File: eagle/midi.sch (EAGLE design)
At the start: 29 parts, among them CON1 EXPANSION-PORT, IC1 74LS14, IC2 6N138, IC4 74LS02, IC5 74LS74, IC6 74AHCT1G32DBV, IC7 74LS273, IC8 SST39SF040, IC9 74LS00D, Q1 2MHz

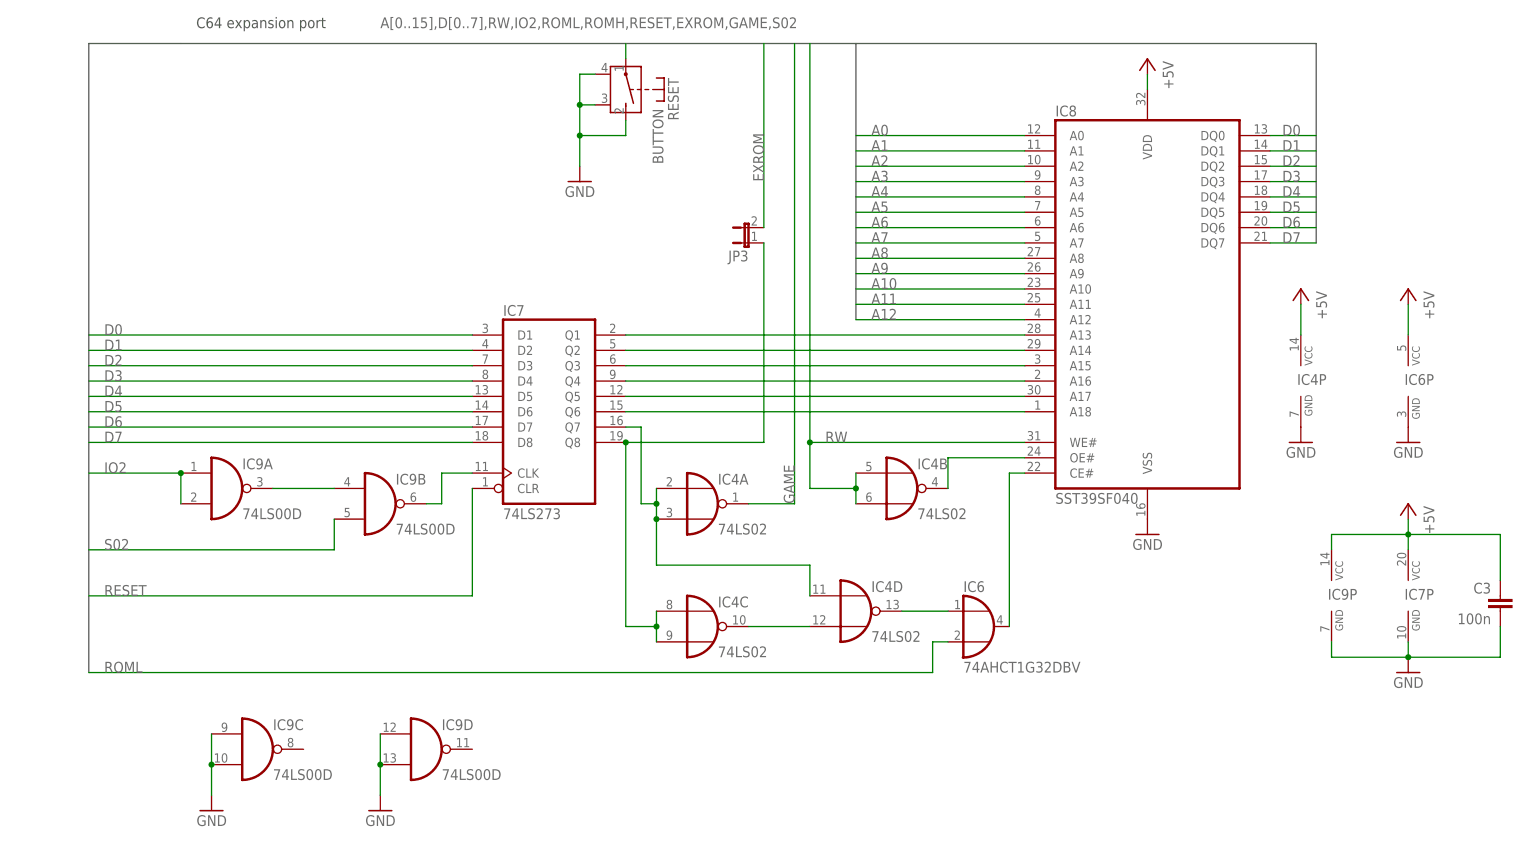
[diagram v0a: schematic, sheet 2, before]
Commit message: version 0.5 with additonal 74LS00
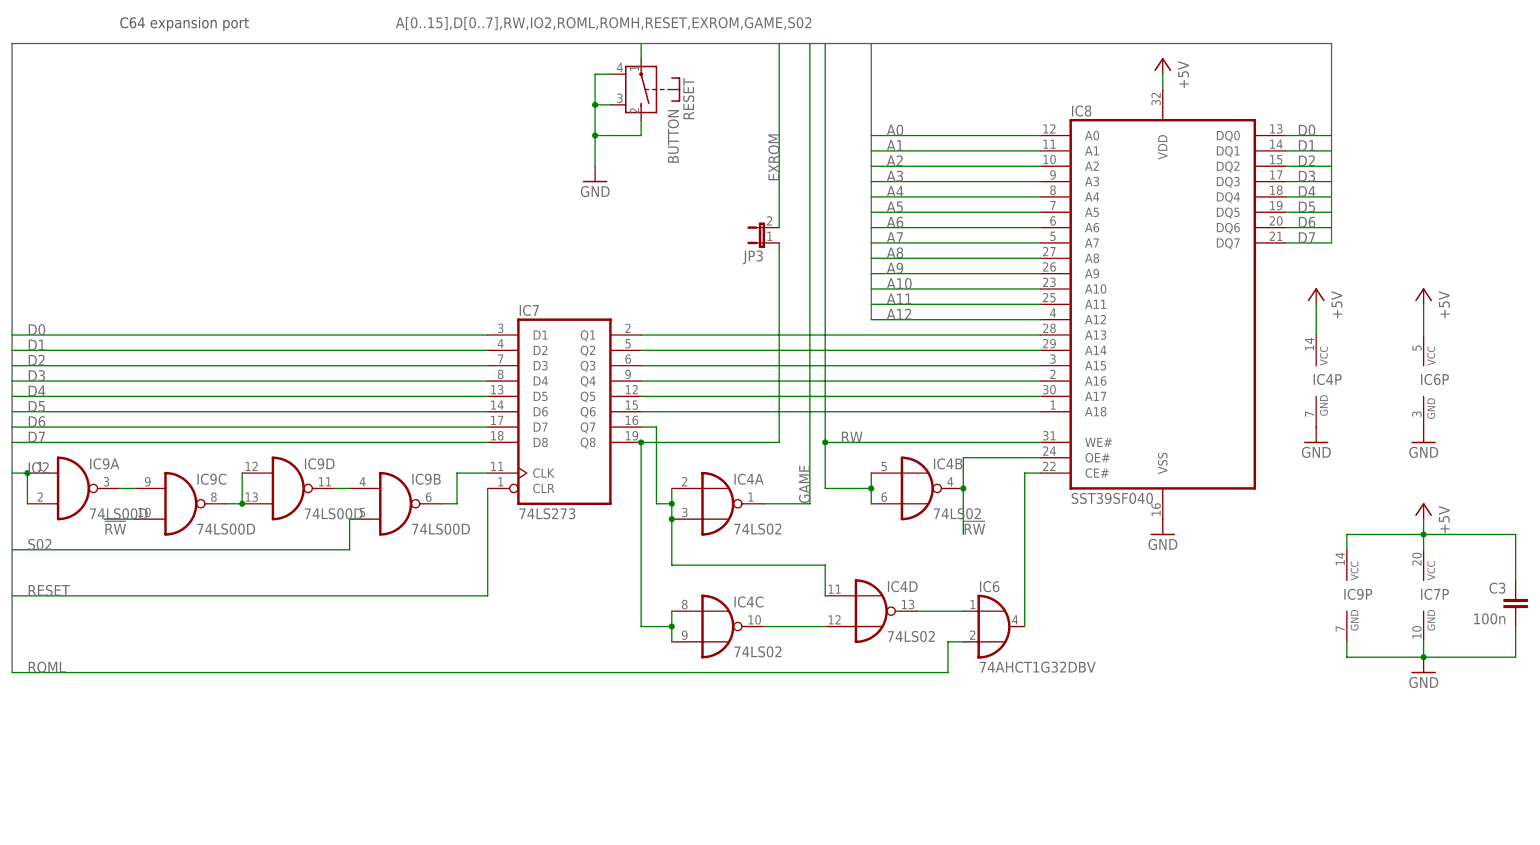
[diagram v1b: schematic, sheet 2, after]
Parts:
- added C4: 10u, rcl:C-EU050-035X075
- added Q2: DMP2100U, transistor-power:FDN360P
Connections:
- removed net OE: IC4B.O, IC8.OE#
- removed net ROMH: CON1.!ROMH
- new net !RW: IC4B.O, IC8.OE#, IC9C.I1
- new net 5V-SW: C1.1, IC3A.CS0, IC3A.CS1, IC3P.VCC, IC5A.CLR, IC5A.PRE, IC5B.CLR, IC5B.PRE, IC5P.VCC, Q1.VCC, Q2.D
- new net N$30: IC9B.I0, IC9D.O
- new net N$35: IC1B.O, Q2.G
- new net N$9: IC9C.O, IC9D.I0, IC9D.I1
- net +5V: now also C4.1, Q2.S; no longer C1.1, IC3A.CS0, IC3A.CS1, IC3P.VCC, IC5A.CLR, IC5A.PRE, IC5B.CLR, IC5B.PRE, IC5P.VCC, Q1.VCC
- net GND: now also C4.2; no longer IC1B.I, IC9C.I0, IC9C.I1, IC9D.I0, IC9D.I1
- net N$8: now also IC9C.I0; no longer IC9B.I0
- net RESET: now also IC1B.I
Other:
- moved on the sheet: C1, C2, C3, IC1B, IC1P, IC3P, IC4A, IC4B, IC4C, IC4D, IC4P, IC6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

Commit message: revision 1.0
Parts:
- added C10, C5, C6, C7, C8, C9: 100n, rcl:C-EUC0805
- added C11, C12: 1n, rcl:C-EUC0805
- added D2, D3: BAV99, diode:BAV199
- added R7: 10k, rcl:R-EU_R0805
- C1, C2, C3: device rcl:C-EU025-025X050 -> rcl:C-EUC0805
- C4: device rcl:C-EU050-035X075 -> rcl:C-EUC0805
- D1: value 1N914 -> BAV99; device diode:1N4148DO35-7 -> diode:BAV199
- R1, R2, R3, R4, R5, R6: device rcl:R-EU_0204/7 -> rcl:R-EU_R1206
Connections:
- removed net N$2: D1.C, IC2.A, R4.1
- new net N$37: D1.AC, D1.C, IC2.A, R4.1
- net +5V: now also C10.1, C7.1, C8.1, C9.1, D2.C, D3.C, R7.1
- net 5V-SW: now also C5.1, C6.1
- net GND: now also C10.2, C11.2, C12.2, C5.2, C6.2, C7.2, C8.2, C9.2, D2.A, D3.A
- net N$16: now also C12.1, D3.AC
- net N$28: now also C11.1, D2.AC
- net N$35: now also R7.2
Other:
- moved on the sheet: IC1D, IC1E, R1, R2

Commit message: circuit rev B with CPLD
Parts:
- removed C10, C2, C5, C6, C7, C8, C9: 100n, rcl:C-EUC0805
- removed C11, C12: 1n, rcl:C-EUC0805
- removed C4: 10u, rcl:C-EUC0805
- removed CON1: EXPANSION-PORT, cartridge:EXPANSION-PORT
- removed D1, D2, D3: BAV99, diode:BAV199
- removed IC6: 74AHCT1G32DBV, 74xx-little-de:74AHCT1G32DBV
- removed IC7: 74LS273, 74xx-eu:74AC273DW
- removed IC8: SST39SF040, flash:SST39SF040
- removed IC9: 74LS00D, 74xx-eu:74LS00D
- removed JP2, JP4: (no value), jumper:JP2E
- removed JP3: (no value), jumper:JP1E
- removed Q1: 2MHz, crystal:XO-14
- removed Q2: DMP2100U, transistor-power:FDN360P
- removed RESET: BUTTON, button:BUTTON
- added 3V3, AUX, GND, TCK, TDI, TDO, TMS: LSP10, solpad:LSP10
- added C13, C14, C17, C18, C19, C20, C21, C26, C28, C37: 100n, rcl:C-EUC0402
- added C15, C16: 1n, rcl:C-EUC0402
- added C22: 10u, rcl:C-EUC0805
- added C24: 1u, rcl:C-EUC0805
- added CON2: EXPANSION-PORT, cartridge:EXPANSION-PORT
- added D4, D5, D6: BAV99, diode:BAV199
- added IC11: (no value), micro-motorola:6850
- added IC12: 74LS14, 74xx-eu:74LS14D
- added IC16: 74LVC8T245, 74lvc8t245:74LVC8T245
- added IC18: MCP1703CB, linear:MCP1703CB
- added LED1, LED2: (no value), led:LED3MM
- added R10, R11, R12, R13, R8, R9: 220, rcl:R-EU_R1206
- added R14, R17, R18: 10k, rcl:R-EU_R0402
- added R15, R16: 4k7, rcl:R-EU_R0402
- added RESET1: BUTTON, button:BUTTON
- C1, C3: device rcl:C-EUC0805 -> rcl:C-EUC0402
- IC1: value 74LS14 -> SST39VF1681; device 74xx-eu:74LS14D -> flash:SST39VF1681
- IC2: value 6N138 -> XC9572XL_TQ100; device optocoupler:6N138 -> xc9572xl-tq100:XC9572XL_TQ100
- IC3: value (none) -> 6N138SMD; device micro-motorola:6850 -> 6n138:6N138SMD
- IC4: value 74LS02 -> 12MHz; device 74xx-eu:74AC02D -> cartridge:ASE
- IC5: value 74LS74 -> CY61228EV30; device 74xx-eu:74LS74D -> CY62128EV30:CY61228EV30
- JP1: device jumper:JP2E -> jumper:JP1E
- R1, R2, R3: value 220 -> 10k; device rcl:R-EU_R1206 -> rcl:R-EU_R0402
- R4, R5: value 220 -> 1k; device rcl:R-EU_R1206 -> rcl:R-EU_R0402
- R6: value 330 -> 10k; device rcl:R-EU_R1206 -> rcl:R-EU_R0402
- R7: value 10k -> 220; device rcl:R-EU_R0805 -> rcl:R-EU_R1206
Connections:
- removed net !RW: IC4B.O, IC8.OE#, IC9C.I1
- removed net 5V-SW: C1.1, C5.1, C6.1, IC3A.CS0, IC3A.CS1, IC3P.VCC, IC5A.CLR, IC5A.PRE, IC5B.CLR, IC5B.PRE, IC5P.VCC, Q1.VCC, Q2.D
- removed net CE: IC6A.O, IC8.CE#
- removed net N$10: IC1D.O, R2.2
- removed net N$11: IC1E.I, JP1.2
- removed net N$12: IC1E.O, R1.2
- removed net N$14: IC3A.RXCLK, IC3A.TXCLK, JP2.2
- removed net N$15: IC1C.O, IC3A.RXDATA
- removed net N$16: C12.1, D3.AC, OUT.5, R2.1
- removed net N$17: IC7A.Q1, IC8.A13
- removed net N$19: IC7A.Q3, IC8.A15
- removed net N$20: IC7A.Q4, IC8.A16
- removed net N$21: IC7A.Q5, IC8.A17
- removed net N$22: IC7A.Q6, IC8.A18
- removed net N$23: IC7A.CLK, IC9B.O
- removed net N$24: IC4C.O, IC4D.I1
- removed net N$25: IC1A.I, IC3A.TXDATA
- removed net N$26: CON1.!IRQ, JP4.3
- removed net N$27: CON1.!NMI, JP4.1
- removed net N$28: C11.1, D2.AC, R1.1, THRU.5
- removed net N$29: IC4D.O, IC6A.I0
- removed net N$30: IC9B.I0, IC9D.O
- removed net N$31: IC5A.!Q, IC5A.D
- removed net N$32: IC5B.!Q, IC5B.D
- removed net N$33: IC5A.CLK, JP2.1, Q1.OUT
- removed net N$34: IC5A.Q, IC5B.CLK
- removed net N$35: IC1B.O, Q2.G, R7.2
- removed net N$36: IC5B.Q, JP2.3
- removed net N$37: D1.AC, D1.C, IC2.A, R4.1
- removed net N$9: IC9C.O, IC9D.I0, IC9D.I1
- removed net Q7: IC4A.I0, IC4A.I1, IC4D.I0, IC7A.Q7
- removed net Q8: IC4C.I0, IC4C.I1, IC7A.Q8, JP3.1
- new net +3V3: 3V3.MP, C1.1, C17.1, C18.1, C19.1, C24.1, C26.1, C28.1, C3.1, C37.1, IC1.!RST, IC1.VDD@1, IC16.VCCA, IC18.VO, IC2.VCCINT_1, IC2.VCCINT_2, IC2.VCCINT_VPP, IC2.VCCIO_1, IC2.VCCIO_2, IC2.VCCIO_3, IC2.VCCIO_4, IC4.VDD, IC5.CE2, IC5.VCC, R14.2, R15.1, R16.1, R18.2, R2.1
- new net 6850-CS2: IC11A.CS2, IC2.PB02_12, R1.1
- new net 6850-IRQ: IC11A.IRQ, IC2.PB02_16
- new net 6850-RS: IC11A.RS, IC2.PB02_15
- new net 6850-RW: IC11A.R/!W, IC2.PB03_00
- new net 6850-RX/TX-CLK: IC11A.RXCLK, IC11A.TXCLK, IC2.PB02_13
- new net 6850-RXDATA: IC11A.RXDATA, IC12F.O, IC2.PB02_06
- new net 6850-TXDATA: IC11A.TXDATA, IC12E.I, IC2.PB02_14
- new net A13: CON2.A13, IC2.PB03_06
- new net A14: CON2.A14, IC2.PB03_10
- new net A15: CON2.A15, IC2.PB03_02
- new net AT0: IC1.A0, IC2.PB00_04, IC5.A0
- new net AT1: IC1.A1, IC2.PB00_01, IC5.A1
- new net AT10: IC1.A10, IC2.PB00_00, IC5.A10
- new net AT11: IC1.A11, IC2.PB00_08, IC5.A14
- new net AT12: IC1.A12, IC2.PB00_10, IC5.A12
- new net AT13: IC1.A13, IC2.PB00_06, IC5.A7
- new net AT14: IC1.A14, IC2.PB00_09, IC5.A6
- new net AT15: IC1.A15, IC2.PB00_14, IC5.A5
- new net AT16: IC1.A16, IC2.PB00_16, IC5.A4
- new net AT17: IC1.A17, IC2.PB02_17
- new net AT18: IC1.A18, IC2.PB02_07
- new net AT19: IC1.A19, IC2.PB00_12
- new net AT2: IC1.A2, IC2.PB01_16, IC5.A2
- new net AT20: IC1.A20, IC2.PB00_11
- new net AT3: IC1.A3, IC2.PB01_14, IC5.A3
- new net AT4: IC1.A4, IC2.PB00_03, IC5.A16
- new net AT5: IC1.A5, IC2.PB02_08, IC5.A11
- new net AT6: IC1.A6, IC2.PB02_00, IC5.A9
- new net AT7: IC1.A7, IC2.PB00_17, IC5.A8
- new net AT8: IC1.A8, IC2.PB00_15, IC5.A13
- new net AT9: IC1.A9, IC2.PB02_01, IC5.A15
- new net BA: CON2.BA
- new net DIR: IC16.DIR, IC2.PB01_09, R17.1
- new net DMA: CON2.!DMA
- new net DOT-CLOCK: CON2.DOT-CLOCK
- new net DT0: IC1.D0, IC16.A1, IC2.PB01_06, IC5.D7
- new net DT1: IC1.D1, IC16.A2, IC2.PB01_10, IC5.D6
- new net DT2: IC1.D2, IC16.A3, IC2.PB01_11, IC5.D5
- new net DT3: IC1.D3, IC16.A4, IC2.PB01_12, IC5.D4
- new net DT4: IC1.D4, IC16.A5, IC2.PB01_13, IC5.D3
- new net DT5: IC1.D5, IC16.A6, IC2.PB01_15, IC5.D2
- new net DT6: IC1.D6, IC16.A7, IC2.PB00_02, IC5.D1
- new net DT7: IC1.D7, IC16.A8, IC2.PB00_07, IC5.D0
- new net FLASH-CE: IC1.!CE, IC2.PB02_09, R14.1
- new net LED1: IC2.PB02_05, R4.1
- new net LED2: IC2.PB02_10, R5.1
- new net MIDI-OUT-INVERTED: IC12C.I, IC12E.O
- new net MIDI-THRU: IC12A.I, IC2.PB02_02
- new net N$2: IC2.PB00_13, IC4.OUT
- new net N$38: IN.4, R8.2
- new net N$39: IC12D.I, IC3.VO, R7.2
- new net N$40: OUT.4, R11.1
- new net N$41: R10.1, THRU.4
- new net N$42: C16.1, D6.AC, OUT.5, R13.1
- new net N$43: C15.1, D5.AC, R12.1, THRU.5
- new net N$44: IC12C.O, R13.2
- new net N$45: IC12B.O, R12.2
- new net N$47: D4.A, IC3.C, IN.5
- new net N$48: D4.AC, D4.C, IC3.A, R8.1
- new net NMI: CON2.!NMI, IC2.PB03_04
- new net OE: IC1.!OE, IC2.PB02_11, IC5.!OE
- new net RAM-CE: IC2.PB00_05, IC5.!CE1, R18.1
- new net ROMH: CON2.!ROMH, IC2.PB03_08
- new net TCK: IC2.TCK, TCK.MP
- new net TDI: IC2.TDI, R15.2, TDI.MP
- new net TDO: IC2.TDO, TDO.MP
- new net TMS: IC2.TMS, R16.2, TMS.MP
- new net WE: IC1.!WE, IC2.PB02_04, IC5.!WE
- net +5V: now also C13.1, C14.1, C20.1, C21.1, C22.1, CON2.+5V1, CON2.+5V2, D5.C, D6.C, IC11A.CS0, IC11A.CS1, IC11P.VCC, IC12P.VCC, IC16.VCCB, IC16.VCCB2, IC18.VI, IC3.VCC, R1.2, R10.2, R11.2, R9.1; no longer C10.1, C2.1, C3.1, C4.1, C7.1, C8.1, C9.1, CON1.+5V1, CON1.+5V2, D2.C, D3.C, IC1P.VCC, IC2.VCC, IC4P.VCC, IC6P.VCC, IC7P.VCC, IC8.VDD, IC9P.VCC, Q2.S, R3.2, R5.2, R6.2, R7.1
- net A0: now also CON2.A0, IC2.PB01_08; no longer CON1.A0, IC3A.RS, IC8.A0
- net A1: now also CON2.A1, IC2.PB01_07; no longer CON1.A1, IC8.A1
- net A10: now also CON2.A10, IC2.PB03_15; no longer CON1.A10, IC8.A10
- net A11: now also CON2.A11, IC2.PB03_11; no longer CON1.A11, IC8.A11
- net A12: now also CON2.A12, IC2.PB03_17; no longer CON1.A12, IC8.A12
- net A2: now also CON2.A2, IC2.PB01_05; no longer CON1.A2, IC8.A2
- net A3: now also CON2.A3, IC2.PB01_04; no longer CON1.A3, IC8.A3
- net A4: now also CON2.A4, IC2.PB01_01; no longer CON1.A4, IC8.A4
- net A5: now also CON2.A5, IC2.PB01_03; no longer CON1.A5, IC8.A5
- net A6: now also CON2.A6, IC2.PB01_17; no longer CON1.A6, IC8.A6
- net A7: now also CON2.A7, IC2.PB01_02; no longer CON1.A7, IC8.A7
- net A8: now also CON2.A8, IC2.PB03_16; no longer CON1.A8, IC8.A8
- net A9: now also CON2.A9, IC2.PB03_14; no longer CON1.A9, IC8.A9
- net D0: now also CON2.D0, IC11A.D0, IC16.B1; no longer CON1.D0, IC3A.D0, IC7A.D1, IC8.DQ0
- net D1: now also CON2.D1, IC11A.D1, IC16.B2; no longer CON1.D1, IC3A.D1, IC7A.D2, IC8.DQ1
- net D2: now also CON2.D2, IC11A.D2, IC16.B3; no longer CON1.D2, IC3A.D2, IC7A.D3, IC8.DQ2
- net D3: now also CON2.D3, IC11A.D3, IC16.B4; no longer CON1.D3, IC3A.D3, IC7A.D4, IC8.DQ3
- net D4: now also CON2.D4, IC11A.D4, IC16.B5; no longer CON1.D4, IC3A.D4, IC7A.D5, IC8.DQ4
- net D5: now also CON2.D5, IC11A.D5, IC16.B6; no longer CON1.D5, IC3A.D5, IC7A.D6, IC8.DQ5
- net D6: now also CON2.D6, IC11A.D6, IC16.B7; no longer CON1.D6, IC3A.D6, IC7A.D7, IC8.DQ6
- net D7: now also CON2.D7, IC11A.D7, IC16.B8; no longer CON1.D7, IC3A.D7, IC7A.D8, IC8.DQ7
- net EXROM: now also CON2.!EXROM, JP1.1; no longer CON1.!EXROM, JP3.2
- net GAME: now also CON2.!GAME, IC2.PB03_13; no longer CON1.!GAME, IC4A.O
- net GND: now also C13.2, C14.2, C15.2, C16.2, C17.2, C18.2, C19.2, C20.2, C21.2, C22.2, C24.2, C26.2, C28.2, C37.2, CON2.GND1, CON2.GND2, CON2.GND3, CON2.GND4, D5.A, D6.A, GND.MP, IC1.GND@1, IC1.GND@2, IC11A.CTS, IC11A.DCD, IC11P.VSS, IC12P.GND, IC16.GND, IC16.GND2, IC16.GND3, IC16.OE, IC18.GND, IC2.VSSINT_1, IC2.VSSINT_2, IC2.VSSINT_3, IC2.VSSIO_1, IC2.VSSIO_2, IC2.VSSIO_3, IC2.VSSIO_4, IC2.VSSIO_5, IC3.GND, IC4.GND, IC5.GND, LED1.C, LED2.C, R17.2, R3.2, R6.1, RESET1.2, RESET1.3, RESET1.4; no longer C10.2, C11.2, C12.2, C2.2, C4.2, C5.2, C6.2, C7.2, C8.2, C9.2, CON1.GND1, CON1.GND2, CON1.GND3, CON1.GND4, D2.A, D3.A, IC1P.GND, IC2.GND, IC3A.CTS, IC3A.DCD, IC3P.VSS, IC4P.GND, IC5P.GND, IC6P.GND, IC7P.GND, IC8.VSS, IC9P.GND, Q1.GND, RESET.2, RESET.3, RESET.4
- net IO1: now also CON2.I/O1, IC2.PB03_05; no longer CON1.I/O1, IC3A.CS2
- net IO2: now also CON2.I/O2, IC2.PB03_12; no longer CON1.I/O2, IC9A.I0, IC9A.I1
- net IRQ: now also CON2.!IRQ, IC2.PB03_07; no longer IC3A.IRQ, JP4.2
- net N$1: now also IC3.VB, R6.2; no longer IN.4, R4.2
- net N$13: now also IC1.!WP, R2.2, R3.1; no longer IC1A.O, IC1D.I, JP1.3
- net N$18: now also LED2.A, R5.2; no longer IC7A.Q2, IC8.A14
- net N$3: now also R7.1, R9.2; no longer D1.A, IC2.C, IN.5
- net N$4: now also IC12A.O, IC12B.I; no longer IC1F.I, IC2.VO, R6.1
- net N$5: now also IC12D.O, IC12F.I; no longer IC1C.I, IC1F.O, JP1.1
- net N$6: now also LED1.A, R4.2; no longer OUT.4, R3.1
- net N$7: now also IC2.PB03_09, JP1.2; no longer R5.1, THRU.4
- net N$8: now also AUX.MP, IC2.PB02_03; no longer IC9A.O, IC9C.I0
- net RESET: now also CON2.!RESET, IC2.PB03_01, RESET1.1; no longer CON1.!RESET, IC1B.I, IC7A.CLR, RESET.1
- net ROML: now also CON2.!ROML, IC2.PB01_00; no longer CON1.!ROML, IC6A.I1
- net RW: now also CON2.R/W, IC2.PB03_03; no longer CON1.R/W, IC3A.R/!W, IC4B.I0, IC4B.I1, IC8.WE#
- net S02: now also CON2.S02, IC11A.E; no longer CON1.S02, IC3A.E, IC9B.I1

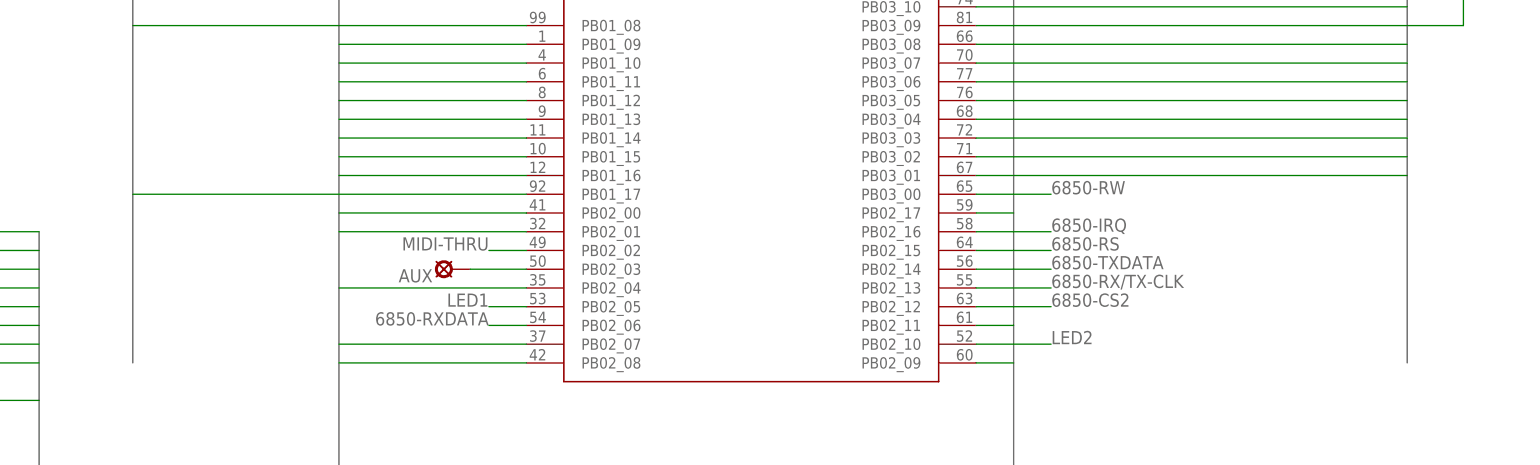
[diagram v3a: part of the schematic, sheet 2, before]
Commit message: first working prototype with CPLD
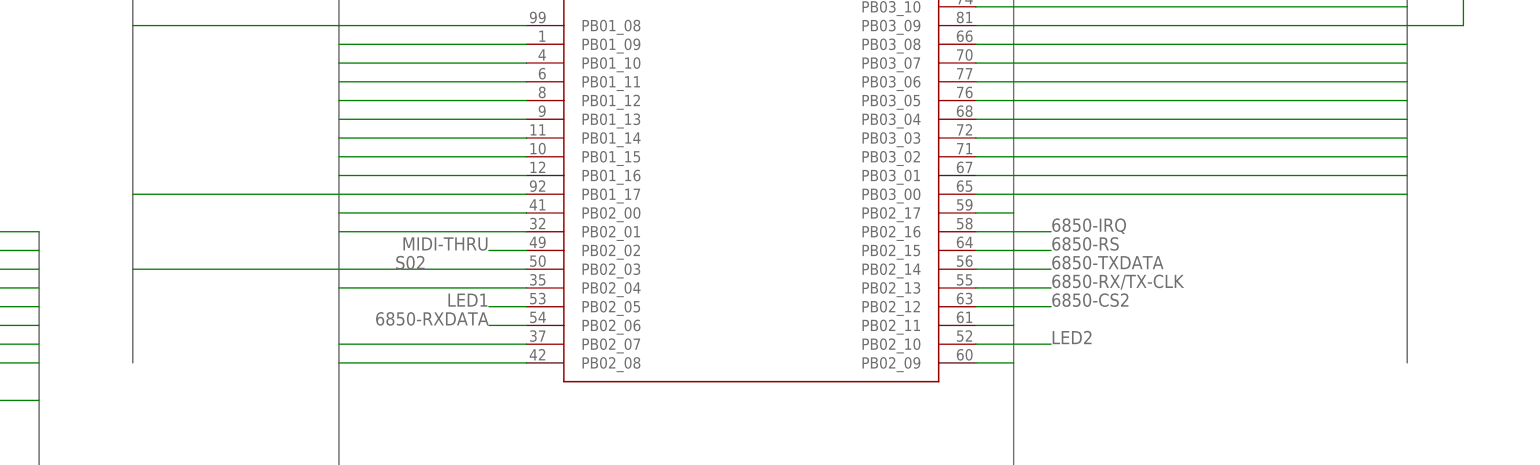
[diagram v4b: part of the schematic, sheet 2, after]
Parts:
- removed AUX: LSP10, solpad:LSP10
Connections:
- removed net 6850-RW: IC11A.R/!W, IC2.PB03_00
- removed net N$8: AUX.MP, IC2.PB02_03
- net BA: now also IC2.PB03_00
- net RW: now also IC11A.R/!W
- net S02: now also IC2.PB02_03

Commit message: new 4 layer board
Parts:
- removed C17, C18, C19, C20, C21, C26, C28, C37: 100n, rcl:C-EUC0402
- removed C22: 10u, rcl:C-EUC0805
- removed IC12: 74LS14, 74xx-eu:74LS14D
- removed IC16: 74LVC8T245, 74lvc8t245:74LVC8T245
- removed IC18: MCP1703CB, linear:MCP1703CB
- removed RESET1: BUTTON, button:BUTTON
- added C10, C12, C4, C5, C6, C7, C8, C9: 100n, rcl:C-EUC0603
- added C2: 1n, rcl:C-EUC0603
- added IC10: EMI-FILTER, emv-filter:EMV-FILTER
- added IC6: XC95144XL_TQ100, xc9572xl-tq100:XC9572XL_TQ100
- added IC7: (no value), micro-motorola:6850
- added IC8: MCP1703DB, mcp1703:MCP1703DB
- added IC9: 74LVC8T245, 74lvc8t245:74LVC8T245
- added R19: 10k, rcl:R-EU_R0603
- added RESET: BUTTON, button:BUTTON
- C1: value 100n -> 1n; device rcl:C-EUC0402 -> rcl:C-EUC0603
- C13, C3: device rcl:C-EUC0402 -> rcl:C-EUC0603
- C14: value 100n -> 10u; device rcl:C-EUC0402 -> rcl:C-EUC0805
- C15, C16: value 1n -> 100n; device rcl:C-EUC0402 -> rcl:C-EUC0603
- IC1: value SST39VF1681 -> 74LS14; device flash:SST39VF1681 -> 74xx-eu:74LS14D
- IC11: value (none) -> EMI-FILTER; device micro-motorola:6850 -> emv-filter:EMV-FILTER
- IC2: value XC9572XL_TQ100 -> SST39VF1681; device xc9572xl-tq100:XC9572XL_TQ100 -> flash:SST39VF1681
- IC4: value 12MHz -> 48MHz
- R1, R2, R3: value 10k -> 220; device rcl:R-EU_R0402 -> rcl:R-EU_R1206
- R10, R12, R8: value 220 -> 10k; device rcl:R-EU_R1206 -> rcl:R-EU_R0603
- R13: value 220 -> 4k7; device rcl:R-EU_R1206 -> rcl:R-EU_R0603
- R14, R17: value 10k -> 4k7; device rcl:R-EU_R0402 -> rcl:R-EU_R0603
- R15, R16: value 4k7 -> 10k; device rcl:R-EU_R0402 -> rcl:R-EU_R0603
- R18: device rcl:R-EU_R0402 -> rcl:R-EU_R0603
- R4, R5: value 1k -> 220; device rcl:R-EU_R0402 -> rcl:R-EU_R1206
- R6: value 10k -> 1k; device rcl:R-EU_R0402 -> rcl:R-EU_R0603
- R7: value 220 -> 1k; device rcl:R-EU_R1206 -> rcl:R-EU_R0603
- renumbered C24 to C11, CON2 to CON1, D4 to D3, D5 to D1, D6 to D2
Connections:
- new net EXROM-F: IC11.10, JP1.1
- new net GAME-F: IC11.12, IC6.PB03_13
- new net IRQ-F: IC11.16, IC6.PB03_07
- new net N$10: IC10.6, IC9.B6
- new net N$11: IC10.5, IC9.B5
- new net N$12: IC10.4, IC9.B4
- new net N$14: IC10.3, IC9.B3
- new net N$15: IC10.2, IC9.B2
- new net N$16: IC10.1, IC9.B1
- new net N$8: IC10.8, IC9.B8
- new net N$9: IC10.7, IC9.B7
- new net NMI-F: IC11.14, IC6.PB03_04
- net +3V3: now also C10.1, C12.1, C13.1, C6.1, C7.1, C8.1, C9.1, IC2.!RST, IC2.VDD@1, IC6.VCCINT_1, IC6.VCCINT_2, IC6.VCCINT_VPP, IC6.VCCIO_1, IC6.VCCIO_2, IC6.VCCIO_3, IC6.VCCIO_4, IC8.VO, IC9.VCCA, R12.2, R13.1, R14.1, R15.2; no longer C1.1, C17.1, C18.1, C19.1, C26.1, C28.1, C37.1, IC1.!RST, IC1.VDD@1, IC16.VCCA, IC18.VO, IC2.VCCINT_1, IC2.VCCINT_2, IC2.VCCINT_VPP, IC2.VCCIO_1, IC2.VCCIO_2, IC2.VCCIO_3, IC2.VCCIO_4, R14.2, R15.1, R16.1, R18.2, R2.1
- net +5V: now also C15.1, C16.1, C4.1, C5.1, IC1P.VCC, IC7A.CS0, IC7A.CS1, IC7P.VCC, IC8.VI, IC9.VCCB, IC9.VCCB2, R17.2, R18.2, R4.2; no longer C13.1, C20.1, C21.1, C22.1, IC11A.CS0, IC11A.CS1, IC11P.VCC, IC12P.VCC, IC16.VCCB, IC16.VCCB2, IC18.VI, R10.2, R11.2
- net 6850-CS2: now also IC6.PB02_12, IC7A.CS2, R18.1; no longer IC11A.CS2, IC2.PB02_12, R1.1
- net 6850-IRQ: now also IC6.PB02_16, IC7A.IRQ, R17.1; no longer IC11A.IRQ, IC2.PB02_16
- net 6850-RS: now also IC6.PB02_15, IC7A.RS; no longer IC11A.RS, IC2.PB02_15
- net 6850-RX/TX-CLK: now also IC6.PB02_13, IC7A.RXCLK, IC7A.TXCLK; no longer IC11A.RXCLK, IC11A.TXCLK, IC2.PB02_13
- net 6850-RXDATA: now also IC1F.O, IC6.PB02_06, IC7A.RXDATA; no longer IC11A.RXDATA, IC12F.O, IC2.PB02_06
- net 6850-TXDATA: now also IC1E.I, IC6.PB02_14, IC7A.TXDATA; no longer IC11A.TXDATA, IC12E.I, IC2.PB02_14
- net A0: now also IC6.PB01_08; no longer IC2.PB01_08
- net A1: now also IC6.PB01_07; no longer IC2.PB01_07
- net A10: now also IC6.PB03_15; no longer IC2.PB03_15
- net A11: now also IC6.PB03_11; no longer IC2.PB03_11
- net A12: now also IC6.PB03_17; no longer IC2.PB03_17
- net A13: now also IC6.PB03_06; no longer IC2.PB03_06
- net A14: now also IC6.PB03_10; no longer IC2.PB03_10
- net A15: now also IC6.PB03_02; no longer IC2.PB03_02
- net A2: now also IC6.PB01_05; no longer IC2.PB01_05
- net A3: now also IC6.PB01_04; no longer IC2.PB01_04
- net A4: now also IC6.PB01_01; no longer IC2.PB01_01
- net A5: now also IC6.PB01_03; no longer IC2.PB01_03
- net A6: now also IC6.PB01_17; no longer IC2.PB01_17
- net A7: now also IC6.PB01_02; no longer IC2.PB01_02
- net A8: now also IC6.PB03_16; no longer IC2.PB03_16
- net A9: now also IC6.PB03_14; no longer IC2.PB03_14
- net AT0: now also IC2.A0, IC6.PB00_04; no longer IC1.A0, IC2.PB00_04
- net AT1: now also IC2.A1, IC6.PB00_01; no longer IC1.A1, IC2.PB00_01
- net AT10: now also IC2.A10, IC6.PB00_00; no longer IC1.A10, IC2.PB00_00
- net AT11: now also IC2.A11, IC6.PB00_08; no longer IC1.A11, IC2.PB00_08
- net AT12: now also IC2.A12, IC6.PB00_10; no longer IC1.A12, IC2.PB00_10
- net AT13: now also IC2.A13, IC6.PB00_06; no longer IC1.A13, IC2.PB00_06
- net AT14: now also IC2.A14, IC6.PB00_09; no longer IC1.A14, IC2.PB00_09
- net AT15: now also IC2.A15, IC6.PB00_14; no longer IC1.A15, IC2.PB00_14
- net AT16: now also IC2.A16, IC6.PB00_16; no longer IC1.A16, IC2.PB00_16
- net AT17: now also IC2.A17, IC6.PB02_17; no longer IC1.A17, IC2.PB02_17
- net AT18: now also IC2.A18, IC6.PB02_07; no longer IC1.A18, IC2.PB02_07
- net AT19: now also IC2.A19, IC6.PB00_12; no longer IC1.A19, IC2.PB00_12
- net AT2: now also IC2.A2, IC6.PB01_16; no longer IC1.A2, IC2.PB01_16
- net AT20: now also IC2.A20, IC6.PB00_11; no longer IC1.A20, IC2.PB00_11
- net AT3: now also IC2.A3, IC6.PB01_14; no longer IC1.A3, IC2.PB01_14
- net AT4: now also IC2.A4, IC6.PB00_03; no longer IC1.A4, IC2.PB00_03
- net AT5: now also IC2.A5, IC6.PB02_08; no longer IC1.A5, IC2.PB02_08
- net AT6: now also IC2.A6, IC6.PB02_00; no longer IC1.A6, IC2.PB02_00
- net AT7: now also IC2.A7, IC6.PB00_17; no longer IC1.A7, IC2.PB00_17
- net AT8: now also IC2.A8, IC6.PB00_15; no longer IC1.A8, IC2.PB00_15
- net AT9: now also IC2.A9, IC6.PB02_01; no longer IC1.A9, IC2.PB02_01
- net BA: now also IC6.PB03_00; no longer IC2.PB03_00
- net D0: now also IC10.16, IC7A.D0; no longer IC11A.D0, IC16.B1
- net D1: now also IC10.15, IC7A.D1; no longer IC11A.D1, IC16.B2
- net D2: now also IC10.14, IC7A.D2; no longer IC11A.D2, IC16.B3
- net D3: now also IC10.13, IC7A.D3; no longer IC11A.D3, IC16.B4
- net D4: now also IC10.12, IC7A.D4; no longer IC11A.D4, IC16.B5
- net D5: now also IC10.11, IC7A.D5; no longer IC11A.D5, IC16.B6
- net D6: now also IC10.10, IC7A.D6; no longer IC11A.D6, IC16.B7
- net D7: now also IC10.9, IC7A.D7; no longer IC11A.D7, IC16.B8
- net DIR: now also IC6.PB01_09, IC9.DIR, R16.1; no longer IC16.DIR, IC2.PB01_09, R17.1
- net DT0: now also IC2.D0, IC6.PB01_06, IC9.A1; no longer IC1.D0, IC16.A1, IC2.PB01_06
- net DT1: now also IC2.D1, IC6.PB01_10, IC9.A2; no longer IC1.D1, IC16.A2, IC2.PB01_10
- net DT2: now also IC2.D2, IC6.PB01_11, IC9.A3; no longer IC1.D2, IC16.A3, IC2.PB01_11
- net DT3: now also IC2.D3, IC6.PB01_12, IC9.A4; no longer IC1.D3, IC16.A4, IC2.PB01_12
- net DT4: now also IC2.D4, IC6.PB01_13, IC9.A5; no longer IC1.D4, IC16.A5, IC2.PB01_13
- net DT5: now also IC2.D5, IC6.PB01_15, IC9.A6; no longer IC1.D5, IC16.A6, IC2.PB01_15
- net DT6: now also IC2.D6, IC6.PB00_02, IC9.A7; no longer IC1.D6, IC16.A7, IC2.PB00_02
- net DT7: now also IC2.D7, IC6.PB00_07, IC9.A8; no longer IC1.D7, IC16.A8, IC2.PB00_07
- net EXROM: now also IC11.7; no longer JP1.1
- net FLASH-CE: now also IC2.!CE, IC6.PB02_09, R12.1; no longer IC1.!CE, IC2.PB02_09, R14.1
- net GAME: now also IC11.5; no longer IC2.PB03_13
- net GND: now also C10.2, C12.2, C2.2, C4.2, C5.2, C6.2, C7.2, C8.2, C9.2, IC10.GND, IC11.GND, IC1P.GND, IC2.GND@1, IC2.GND@2, IC6.VSSINT_1, IC6.VSSINT_2, IC6.VSSINT_3, IC6.VSSIO_1, IC6.VSSIO_2, IC6.VSSIO_3, IC6.VSSIO_4, IC6.VSSIO_5, IC7A.CTS, IC7A.DCD, IC7P.VSS, IC8.GND, IC9.GND, IC9.GND2, IC9.GND3, IC9.OE, R10.1, R16.2, R19.2, R8.2, RESET.2, RESET.3, RESET.4; no longer C17.2, C18.2, C19.2, C20.2, C21.2, C22.2, C26.2, C28.2, C37.2, IC1.GND@1, IC1.GND@2, IC11A.CTS, IC11A.DCD, IC11P.VSS, IC12P.GND, IC16.GND, IC16.GND2, IC16.GND3, IC16.OE, IC18.GND, IC2.VSSINT_1, IC2.VSSINT_2, IC2.VSSINT_3, IC2.VSSIO_1, IC2.VSSIO_2, IC2.VSSIO_3, IC2.VSSIO_4, IC2.VSSIO_5, R17.2, R3.2, R6.1, RESET1.2, RESET1.3, RESET1.4
- net IO1: now also IC6.PB03_05; no longer IC2.PB03_05
- net IO2: now also IC6.PB03_12; no longer IC2.PB03_12
- net IRQ: now also IC11.1; no longer IC2.PB03_07
- net LED1: now also IC6.PB02_05, R6.1; no longer IC2.PB02_05, R4.1
- net LED2: now also IC6.PB02_10, R7.1; no longer IC2.PB02_10, R5.1
- net MIDI-OUT-INVERTED: now also IC1C.I, IC1E.O; no longer IC12C.I, IC12E.O
- net MIDI-THRU: now also IC1A.I, IC6.PB02_02; no longer IC12A.I, IC2.PB02_02
- net N$1: now also R10.2; no longer R6.2
- net N$13: now also IC2.!WP, R8.1; no longer IC1.!WP, R2.2, R3.1
- net N$18: now also R7.2; no longer R5.2
- net N$2: now also IC6.PB00_13; no longer IC2.PB00_13
- net N$3: now also R11.1; no longer R7.1
- net N$38: now also R2.2; no longer R8.2
- net N$39: now also IC1D.I, R11.2; no longer IC12D.I, R7.2
- net N$4: now also IC1A.O, IC1B.I; no longer IC12A.O, IC12B.I
- net N$40: now also R1.1; no longer R11.1
- net N$41: now also R4.1; no longer R10.1
- net N$42: now also C2.1, R5.1; no longer C16.1, R13.1
- net N$43: now also C1.1, R3.1; no longer C15.1, R12.1
- net N$44: now also IC1C.O, R5.2; no longer IC12C.O, R13.2
- net N$45: now also IC1B.O, R3.2; no longer IC12B.O, R12.2
- net N$48: now also R2.1; no longer R8.1
- net N$5: now also IC1D.O, IC1F.I; no longer IC12D.O, IC12F.I
- net N$6: now also R6.2; no longer R4.2
- net N$7: now also IC6.PB03_09, R19.1; no longer IC2.PB03_09
- net NMI: now also IC11.3; no longer IC2.PB03_04
- net OE: now also IC2.!OE, IC6.PB02_11; no longer IC1.!OE, IC2.PB02_11
- net RAM-CE: now also IC6.PB00_05, R15.1; no longer IC2.PB00_05, R18.1
- net RESET: now also IC6.PB03_01, RESET.1; no longer IC2.PB03_01, RESET1.1
- net ROMH: now also IC6.PB03_08; no longer IC2.PB03_08
- net ROML: now also IC6.PB01_00; no longer IC2.PB01_00
- net RW: now also IC6.PB03_03, IC7A.R/!W; no longer IC11A.R/!W, IC2.PB03_03
- net S02: now also IC6.PB02_03, IC7A.E; no longer IC11A.E, IC2.PB02_03
- net TCK: now also IC6.TCK; no longer IC2.TCK
- net TDI: now also IC6.TDI, R13.2; no longer IC2.TDI, R15.2
- net TDO: now also IC6.TDO; no longer IC2.TDO
- net TMS: now also IC6.TMS, R14.2; no longer IC2.TMS, R16.2
- net WE: now also IC2.!WE, IC6.PB02_04; no longer IC1.!WE, IC2.PB02_04
